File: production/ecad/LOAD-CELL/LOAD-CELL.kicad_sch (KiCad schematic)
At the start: 17 parts, among them J10 214721-0061, Q3 MMBT4403, U3 HX711

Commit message: added connector for pisugar
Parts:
- U3: footprint Load Cell and Amplifier:SO16 -> Load Cell and Amplifier:HX711
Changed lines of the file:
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@@
 			)
 		)
-		(property "Footprint" "Load Cell and Amplifier:SO16"
+		(property "Footprint" "Load Cell and Amplifier:HX711"
 			(at 177.8 88.9 0)
 			(effects

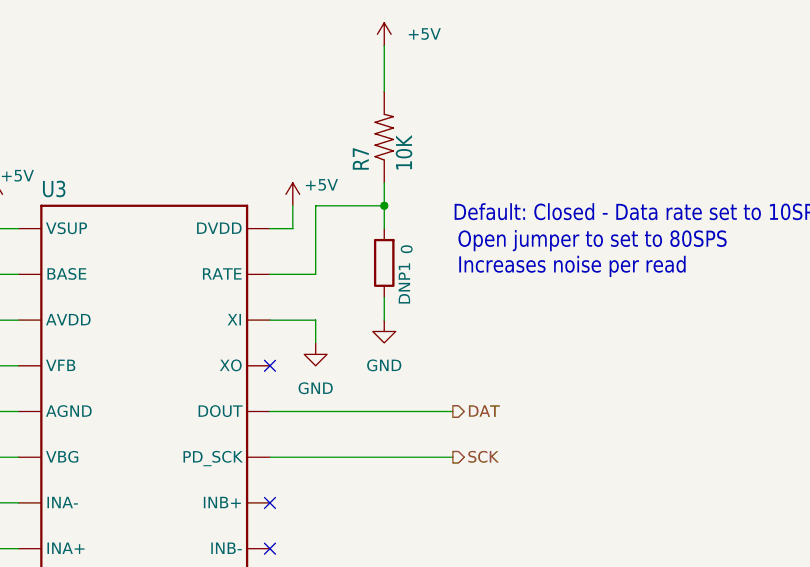
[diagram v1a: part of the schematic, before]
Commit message: Changed 53.6k resistor into two 27k resistors in series (BMS)
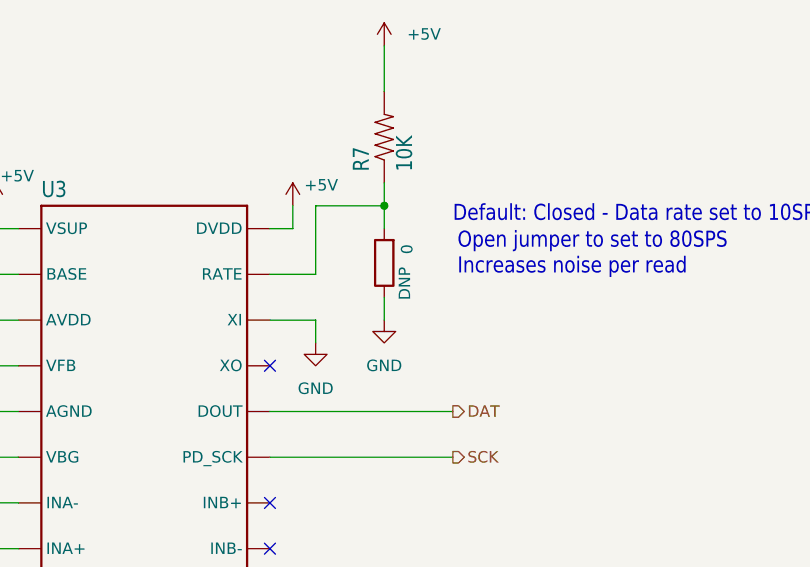
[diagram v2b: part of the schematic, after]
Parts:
- renumbered DNP1 to DNP
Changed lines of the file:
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@@
 		(on_board yes)
 		(dnp no)
-		(property "Reference" "DNP1"
+		(property "Reference" "DNP"
 			(at 205.486 77.216 90)
 			(effects
@@
 			(project "Main"
 				(path "/a34d77bc-8f6a-417e-a206-3165e6c5c658/1fa8e4ec-3b8f-41b7-8956-25ba2b294586"
-					(reference "DNP1")
+					(reference "DNP")
 					(unit 1)
 				)

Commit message: All footprints for components + passives from BMS are assigned and ready for layout
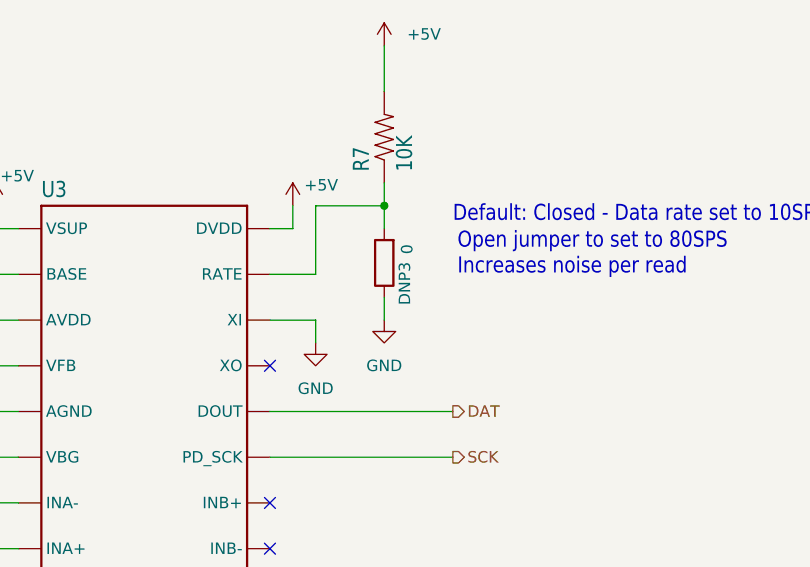
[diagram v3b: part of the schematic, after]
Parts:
- DNP3: renamed from DNP; footprint (none) -> Resistor_SMD:R_0201_0603Metric
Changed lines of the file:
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@@
 		(on_board yes)
 		(dnp no)
-		(property "Reference" "DNP"
+		(property "Reference" "DNP3"
 			(at 205.486 77.216 90)
 			(effects
@@
 			)
 		)
-		(property "Footprint" ""
+		(property "Footprint" "Resistor_SMD:R_0201_0603Metric"
 			(at 204.978 74.93 90)
 			(effects
@@
 			(project "Main"
 				(path "/a34d77bc-8f6a-417e-a206-3165e6c5c658/1fa8e4ec-3b8f-41b7-8956-25ba2b294586"
-					(reference "DNP")
+					(reference "DNP3")
 					(unit 1)
 				)

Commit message: david changes
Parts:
- C3, C4, C6, C8, C9: footprint Load Cell and Amplifier:0603-CAP -> LoadCellFootprints:0p1uF
- C5, C7: footprint Load Cell and Amplifier:1210 -> LoadCellFootprints:10uF
- DNP1: renamed from DNP3; footprint Resistor_SMD:R_0201_0603Metric -> LoadCellFootprints:10k
- J10: footprint 2147210061 -> LoadCellFootprints:6_pos_connector
- L1: footprint Load Cell and Amplifier:0805 -> LoadCellFootprints:inductor
- Q3: footprint Load Cell and Amplifier:SOT23-3 -> LoadCellFootprints:mmbt4403
- R3: footprint Load Cell and Amplifier:0603-RES -> LoadCellFootprints:20k
- R4: footprint Load Cell and Amplifier:0603-RES -> LoadCellFootprints:8p2k
- R5, R6: footprint Load Cell and Amplifier:0603-RES -> LoadCellFootprints:100ohm
- R7: footprint Load Cell and Amplifier:0603-RES -> LoadCellFootprints:10k
- U3: footprint Load Cell and Amplifier:HX711 -> LoadCellFootprints:HX711
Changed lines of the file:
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@@
 		(on_board yes)
 		(dnp no)
-		(property "Reference" "DNP3"
+		(property "Reference" "DNP1"
 			(at 205.486 77.216 90)
 			(effects
@@
 			)
 		)
-		(property "Footprint" "Resistor_SMD:R_0201_0603Metric"
+		(property "Footprint" "LoadCellFootprints:10k"
 			(at 204.978 74.93 90)
 			(effects
@@
 			(project "Main"
 				(path "/a34d77bc-8f6a-417e-a206-3165e6c5c658/1fa8e4ec-3b8f-41b7-8956-25ba2b294586"
-					(reference "DNP3")
+					(reference "DNP1")
 					(unit 1)
 				)
@@
 			)
 		)
-		(property "Footprint" "Load Cell and Amplifier:0603-RES"
+		(property "Footprint" "LoadCellFootprints:100ohm"
 			(at 139.7 111.76 0)
 			(effects
@@
 			)
 		)
-		(property "Footprint" "Load Cell and Amplifier:1210"
+		(property "Footprint" "LoadCellFootprints:10uF"
 			(at 109.22 78.74 0)
 			(effects
@@
 			)
 		)
-		(property "Footprint" "Load Cell and Amplifier:0805"
+		(property "Footprint" "LoadCellFootprints:inductor"
 			(at 124.46 71.12 0)
 			(effects
@@
 			)
 		)
-		(property "Footprint" "Load Cell and Amplifier:HX711"
+		(property "Footprint" "LoadCellFootprints:HX711"
 			(at 177.8 88.9 0)
 			(effects
@@
 			)
 		)
-		(property "Footprint" "Load Cell and Amplifier:0603-RES"
+		(property "Footprint" "LoadCellFootprints:100ohm"
 			(at 139.7 124.46 0)
 			(effects
@@
 			)
 		)
-		(property "Footprint" "Load Cell and Amplifier:0603-CAP"
+		(property "Footprint" "LoadCellFootprints:0p1uF"
 			(at 149.86 101.6 0)
 			(effects
@@
 			)
 		)
-		(property "Footprint" "Load Cell and Amplifier:0603-CAP"
+		(property "Footprint" "LoadCellFootprints:0p1uF"
 			(at 92.71 31.75 0)
 			(effects
@@
 			)
 		)
-		(property "Footprint" "Load Cell and Amplifier:0603-CAP"
+		(property "Footprint" "LoadCellFootprints:0p1uF"
 			(at 147.32 119.38 0)
 			(effects
@@
 			)
 		)
-		(property "Footprint" "Load Cell and Amplifier:0603-RES"
+		(property "Footprint" "LoadCellFootprints:8p2k"
 			(at 137.16 93.98 0)
 			(effects
@@
 			)
 		)
-		(property "Footprint" "Load Cell and Amplifier:SOT23-3"
+		(property "Footprint" "LoadCellFootprints:mmbt4403"
 			(at 144.78 63.5 0)
 			(effects
@@
 			)
 		)
-		(property "Footprint" "2147210061"
+		(property "Footprint" "LoadCellFootprints:6_pos_connector"
 			(at 72.39 166.04 0)
 			(effects
@@
 			)
 		)
-		(property "Footprint" "Load Cell and Amplifier:0603-CAP"
+		(property "Footprint" "LoadCellFootprints:0p1uF"
 			(at 105.41 31.75 0)
 			(effects
@@
 			)
 		)
-		(property "Footprint" "Load Cell and Amplifier:0603-CAP"
+		(property "Footprint" "LoadCellFootprints:0p1uF"
 			(at 99.06 78.74 0)
 			(effects
@@
 			)
 		)
-		(property "Footprint" "Load Cell and Amplifier:0603-RES"
+		(property "Footprint" "LoadCellFootprints:10k"
 			(at 203.2 60.96 0)
 			(effects
@@
 			)
 		)
-		(property "Footprint" "Load Cell and Amplifier:1210"
+		(property "Footprint" "LoadCellFootprints:10uF"
 			(at 120.65 31.75 0)
 			(effects
@@
 			)
 		)
-		(property "Footprint" "Load Cell and Amplifier:0603-RES"
+		(property "Footprint" "LoadCellFootprints:20k"
 			(at 137.16 78.74 0)
 			(effects
